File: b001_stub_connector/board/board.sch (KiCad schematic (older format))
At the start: 10 parts, among them J1 Conn_01x10_Male, J10 Conn_01x10_Male, J2 Conn_01x10_Male, J3 Conn_01x10_Male, J4 Conn_01x10_Male, J5 Conn_01x10_Male, J6 Conn_01x10_Male, J7 Conn_01x10_Male, J8 Conn_01x10_Male, J9 Conn_01x10_Male

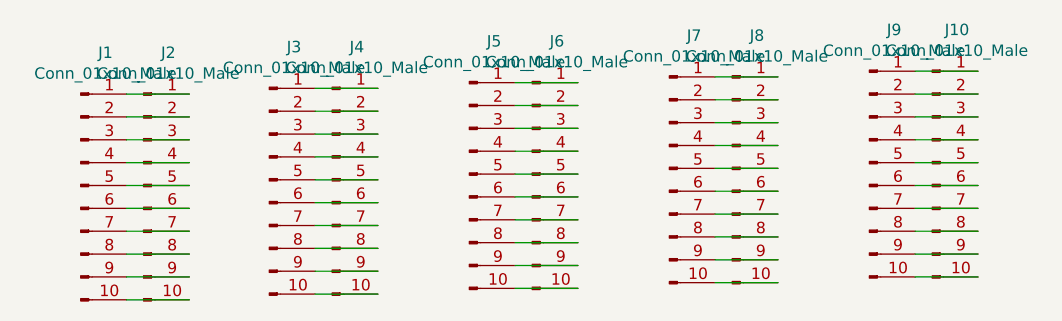
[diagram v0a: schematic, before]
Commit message: added stm32f042 breakout
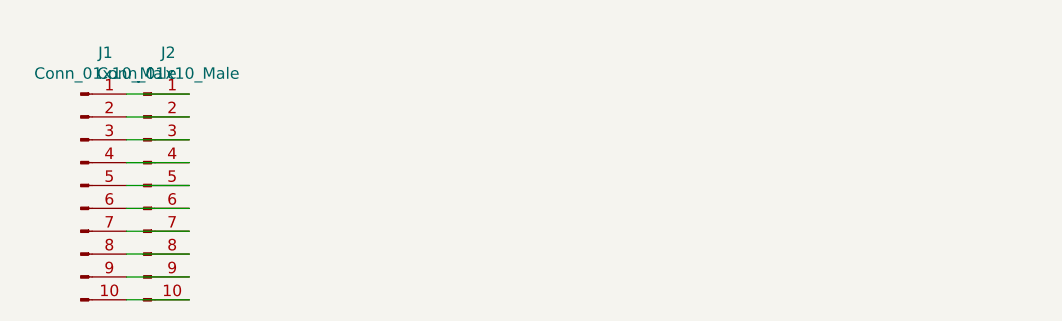
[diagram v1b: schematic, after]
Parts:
- removed J10, J4, J6, J8: Conn_01x10_Male, on_edge:on_edge_2x05_solder, symbol Connector:Conn_01x10_Male
- removed J3, J5, J7, J9: Conn_01x10_Male, on_edge:on_edge_2x05_host, symbol Connector:Conn_01x10_Male
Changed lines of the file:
@@
 Wire Wire Line
 	3900 4500 3625 4500
-$Comp
-L Connector:Conn_01x10_Male J?
-U 1 1 60A862A9
-P 4250 3975
-AR Path="/6029F329/60A862A9" Ref="J?"  Part="1"
-AR Path="/60A862A9" Ref="J3"  Part="1"
-F 0 "J3" H 4358 4556 50  0000 C CNN
-F 1 "Conn_01x10_Male" H 4358 4465 50  0000 C CNN
-F 2 "on_edge:on_edge_2x05_host" H 4250 3975 50  0001 C CNN
-F 3 "~" H 4250 3975 50  0001 C CNN
-	1    4250 3975
-	1    0    0    -1
-$EndComp
-$Comp
-L Connector:Conn_01x10_Male J?
-U 1 1 60A862AF
-P 4525 3975
-AR Path="/6029F329/60A862AF" Ref="J?"  Part="1"
-AR Path="/60A862AF" Ref="J4"  Part="1"
-F 0 "J4" H 4633 4556 50  0000 C CNN
-F 1 "Conn_01x10_Male" H 4633 4465 50  0000 C CNN
-F 2 "on_edge:on_edge_2x05_solder" H 4525 3975 50  0001 C CNN
-F 3 "~" H 4525 3975 50  0001 C CNN
-	1    4525 3975
-	1    0    0    -1
-$EndComp
-Wire Wire Line
-	4450 3575 4725 3575
-Wire Wire Line
-	4725 3675 4450 3675
-Wire Wire Line
-	4450 3775 4725 3775
-Wire Wire Line
-	4725 3875 4450 3875
-Wire Wire Line
-	4450 3975 4725 3975
-Wire Wire Line
-	4725 4075 4450 4075
-Wire Wire Line
-	4450 4175 4725 4175
-Wire Wire Line
-	4725 4275 4450 4275
-Wire Wire Line
-	4450 4375 4725 4375
-Wire Wire Line
-	4725 4475 4450 4475
-$Comp
-L Connector:Conn_01x10_Male J?
-U 1 1 60A87827
-P 5125 3950
-AR Path="/6029F329/60A87827" Ref="J?"  Part="1"
-AR Path="/60A87827" Ref="J5"  Part="1"
-F 0 "J5" H 5233 4531 50  0000 C CNN
-F 1 "Conn_01x10_Male" H 5233 4440 50  0000 C CNN
-F 2 "on_edge:on_edge_2x05_host" H 5125 3950 50  0001 C CNN
-F 3 "~" H 5125 3950 50  0001 C CNN
-	1    5125 3950
-	1    0    0    -1
-$EndComp
-$Comp
-L Connector:Conn_01x10_Male J?
-U 1 1 60A8782D
-P 5400 3950
-AR Path="/6029F329/60A8782D" Ref="J?"  Part="1"
-AR Path="/60A8782D" Ref="J6"  Part="1"
-F 0 "J6" H 5508 4531 50  0000 C CNN
-F 1 "Conn_01x10_Male" H 5508 4440 50  0000 C CNN
-F 2 "on_edge:on_edge_2x05_solder" H 5400 3950 50  0001 C CNN
-F 3 "~" H 5400 3950 50  0001 C CNN
-	1    5400 3950
-	1    0    0    -1
-$EndComp
-Wire Wire Line
-	5325 3550 5600 3550
-Wire Wire Line
-	5600 3650 5325 3650
-Wire Wire Line
-	5325 3750 5600 3750
-Wire Wire Line
-	5600 3850 5325 3850
-Wire Wire Line
-	5325 3950 5600 3950
-Wire Wire Line
-	5600 4050 5325 4050
-Wire Wire Line
-	5325 4150 5600 4150
-Wire Wire Line
-	5600 4250 5325 4250
-Wire Wire Line
-	5325 4350 5600 4350
-Wire Wire Line
-	5600 4450 5325 4450
-$Comp
-L Connector:Conn_01x10_Male J?
-U 1 1 60A88950
-P 6000 3925
-AR Path="/6029F329/60A88950" Ref="J?"  Part="1"
-AR Path="/60A88950" Ref="J7"  Part="1"
-F 0 "J7" H 6108 4506 50  0000 C CNN
-F 1 "Conn_01x10_Male" H 6108 4415 50  0000 C CNN
-F 2 "on_edge:on_edge_2x05_host" H 6000 3925 50  0001 C CNN
-F 3 "~" H 6000 3925 50  0001 C CNN
-	1    6000 3925
-	1    0    0    -1
-$EndComp
-$Comp
-L Connector:Conn_01x10_Male J?
-U 1 1 60A88956
-P 6275 3925
-AR Path="/6029F329/60A88956" Ref="J?"  Part="1"
-AR Path="/60A88956" Ref="J8"  Part="1"
-F 0 "J8" H 6383 4506 50  0000 C CNN
-F 1 "Conn_01x10_Male" H 6383 4415 50  0000 C CNN
-F 2 "on_edge:on_edge_2x05_solder" H 6275 3925 50  0001 C CNN
-F 3 "~" H 6275 3925 50  0001 C CNN
-	1    6275 3925
-	1    0    0    -1
-$EndComp
-Wire Wire Line
-	6200 3525 6475 3525
-Wire Wire Line
-	6475 3625 6200 3625
-Wire Wire Line
-	6200 3725 6475 3725
-Wire Wire Line
-	6475 3825 6200 3825
-Wire Wire Line
-	6200 3925 6475 3925
-Wire Wire Line
-	6475 4025 6200 4025
-Wire Wire Line
-	6200 4125 6475 4125
-Wire Wire Line
-	6475 4225 6200 4225
-Wire Wire Line
-	6200 4325 6475 4325
-Wire Wire Line
-	6475 4425 6200 4425
-$Comp
-L Connector:Conn_01x10_Male J?
-U 1 1 60A8A6D0
-P 6875 3900
-AR Path="/6029F329/60A8A6D0" Ref="J?"  Part="1"
-AR Path="/60A8A6D0" Ref="J9"  Part="1"
-F 0 "J9" H 6983 4481 50  0000 C CNN
-F 1 "Conn_01x10_Male" H 6983 4390 50  0000 C CNN
-F 2 "on_edge:on_edge_2x05_host" H 6875 3900 50  0001 C CNN
-F 3 "~" H 6875 3900 50  0001 C CNN
-	1    6875 3900
-	1    0    0    -1
-$EndComp
-$Comp
-L Connector:Conn_01x10_Male J?
-U 1 1 60A8A6D6
-P 7150 3900
-AR Path="/6029F329/60A8A6D6" Ref="J?"  Part="1"
-AR Path="/60A8A6D6" Ref="J10"  Part="1"
-F 0 "J10" H 7258 4481 50  0000 C CNN
-F 1 "Conn_01x10_Male" H 7258 4390 50  0000 C CNN
-F 2 "on_edge:on_edge_2x05_solder" H 7150 3900 50  0001 C CNN
-F 3 "~" H 7150 3900 50  0001 C CNN
-	1    7150 3900
-	1    0    0    -1
-$EndComp
-Wire Wire Line
-	7075 3500 7350 3500
-Wire Wire Line
-	7350 3600 7075 3600
-Wire Wire Line
-	7075 3700 7350 3700
-Wire Wire Line
-	7350 3800 7075 3800
-Wire Wire Line
-	7075 3900 7350 3900
-Wire Wire Line
-	7350 4000 7075 4000
-Wire Wire Line
-	7075 4100 7350 4100
-Wire Wire Line
-	7350 4200 7075 4200
-Wire Wire Line
-	7075 4300 7350 4300
-Wire Wire Line
-	7350 4400 7075 4400
 $EndSCHEMATC
